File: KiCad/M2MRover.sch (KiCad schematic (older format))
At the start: 22 parts, among them J1 Light Detection, J10 MPU6050 Gyro & Acc GY-521, J11 microbit_edge_connector, J2 Serial (Bluetooth), J3 Servo, J4 H-Bridge, J5 Ultrasonic Down, J6 Ultrasonic Forward, J7 Compass GY-273, J8 Left Hall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

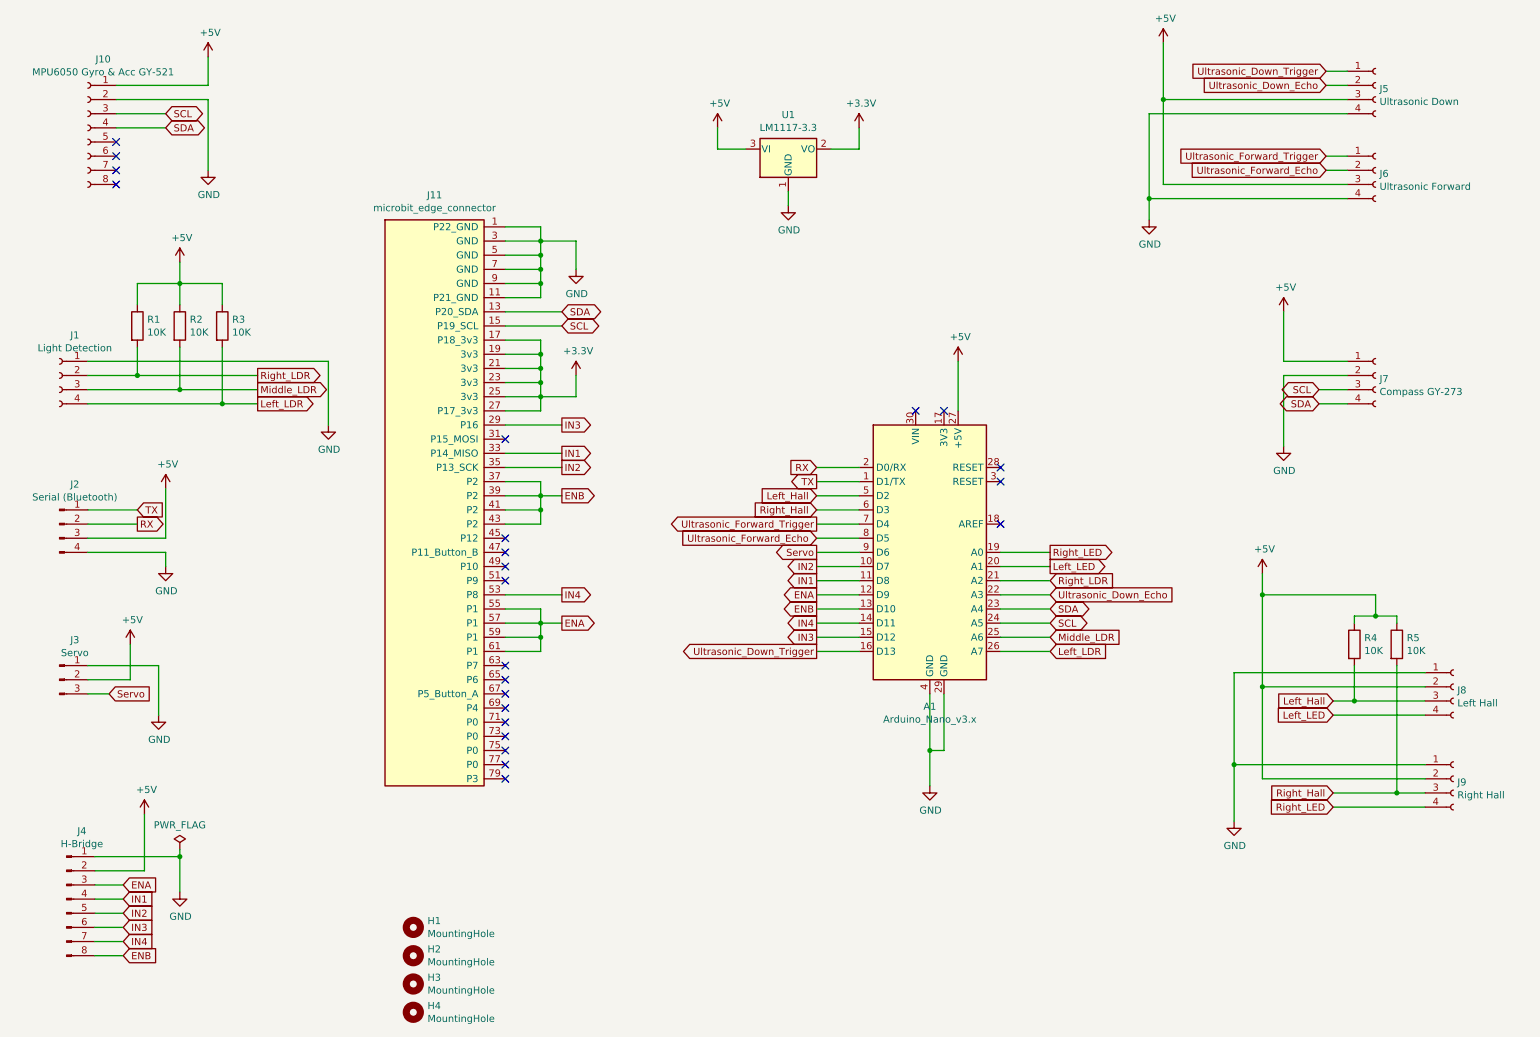
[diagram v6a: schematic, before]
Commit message: Add ESP8266-01 connector
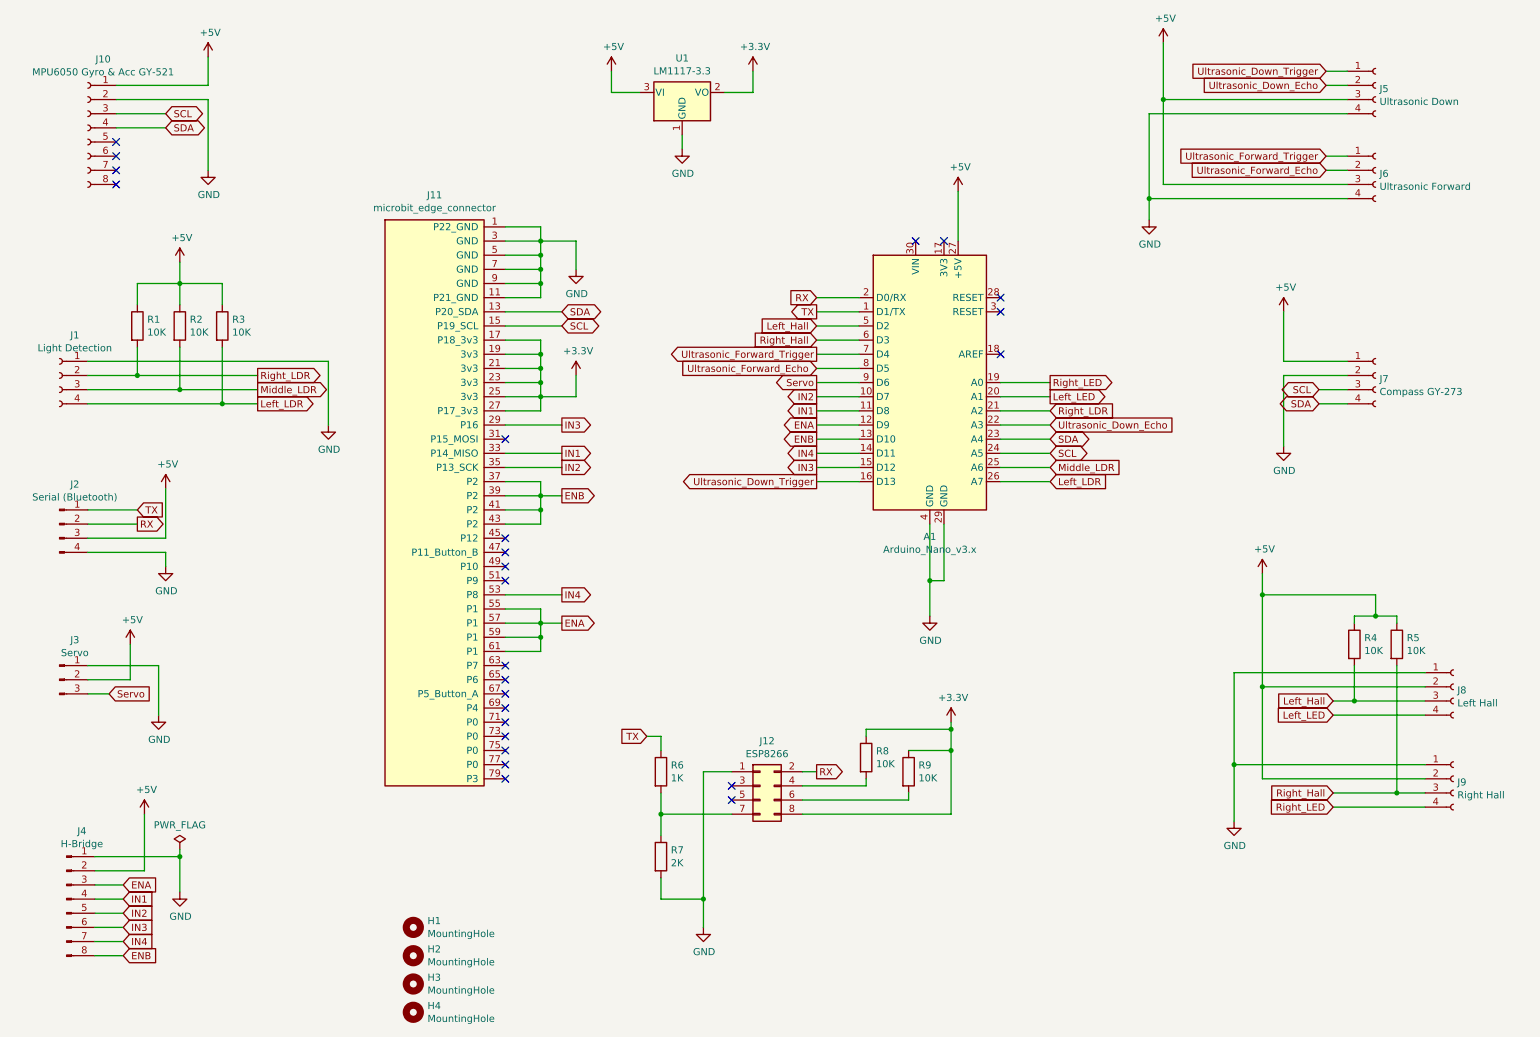
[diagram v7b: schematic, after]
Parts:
- added J12: ESP8266, Connector_PinSocket_2.54mm:PinSocket_2x04_P2.54mm_Vertical, symbol Connector_Generic:Conn_02x04_Odd_Even
- added R6: 1K, symbol Device:R
- added R7: 2K, symbol Device:R
- added R8, R9: 10K, symbol Device:R
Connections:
- net +3V3: now also J12.8 (Pin_8), R8.1, R9.1
- net GND: now also J12.1 (Pin_1), R7.2
- net RX: now also J12.2 (Pin_2)
- net TX: now also R6.1
- new net: J12.4 (Pin_4), R8.2
- new net: J12.6 (Pin_6), R9.2
- new net: J12.7 (Pin_7), R6.2, R7.1
- no-connect marks 23 -> 25
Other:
- moved on the sheet: A1, U1
